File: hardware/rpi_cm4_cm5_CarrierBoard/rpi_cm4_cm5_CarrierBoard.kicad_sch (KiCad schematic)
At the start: 0 parts

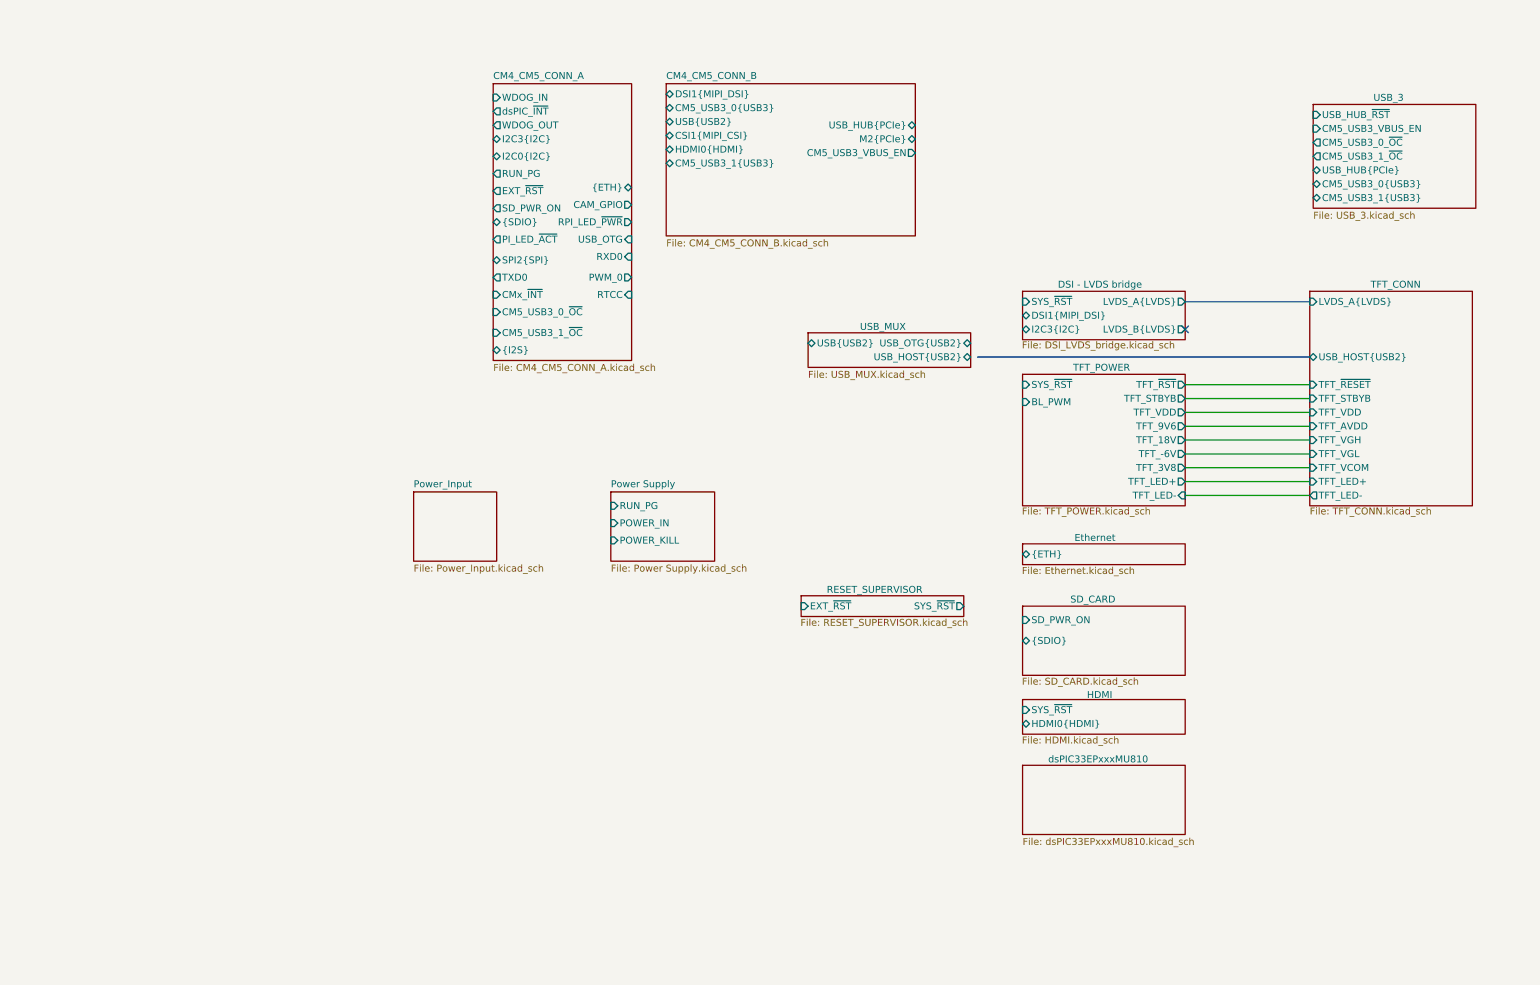
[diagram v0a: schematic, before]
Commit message: Add dsPIC sheet
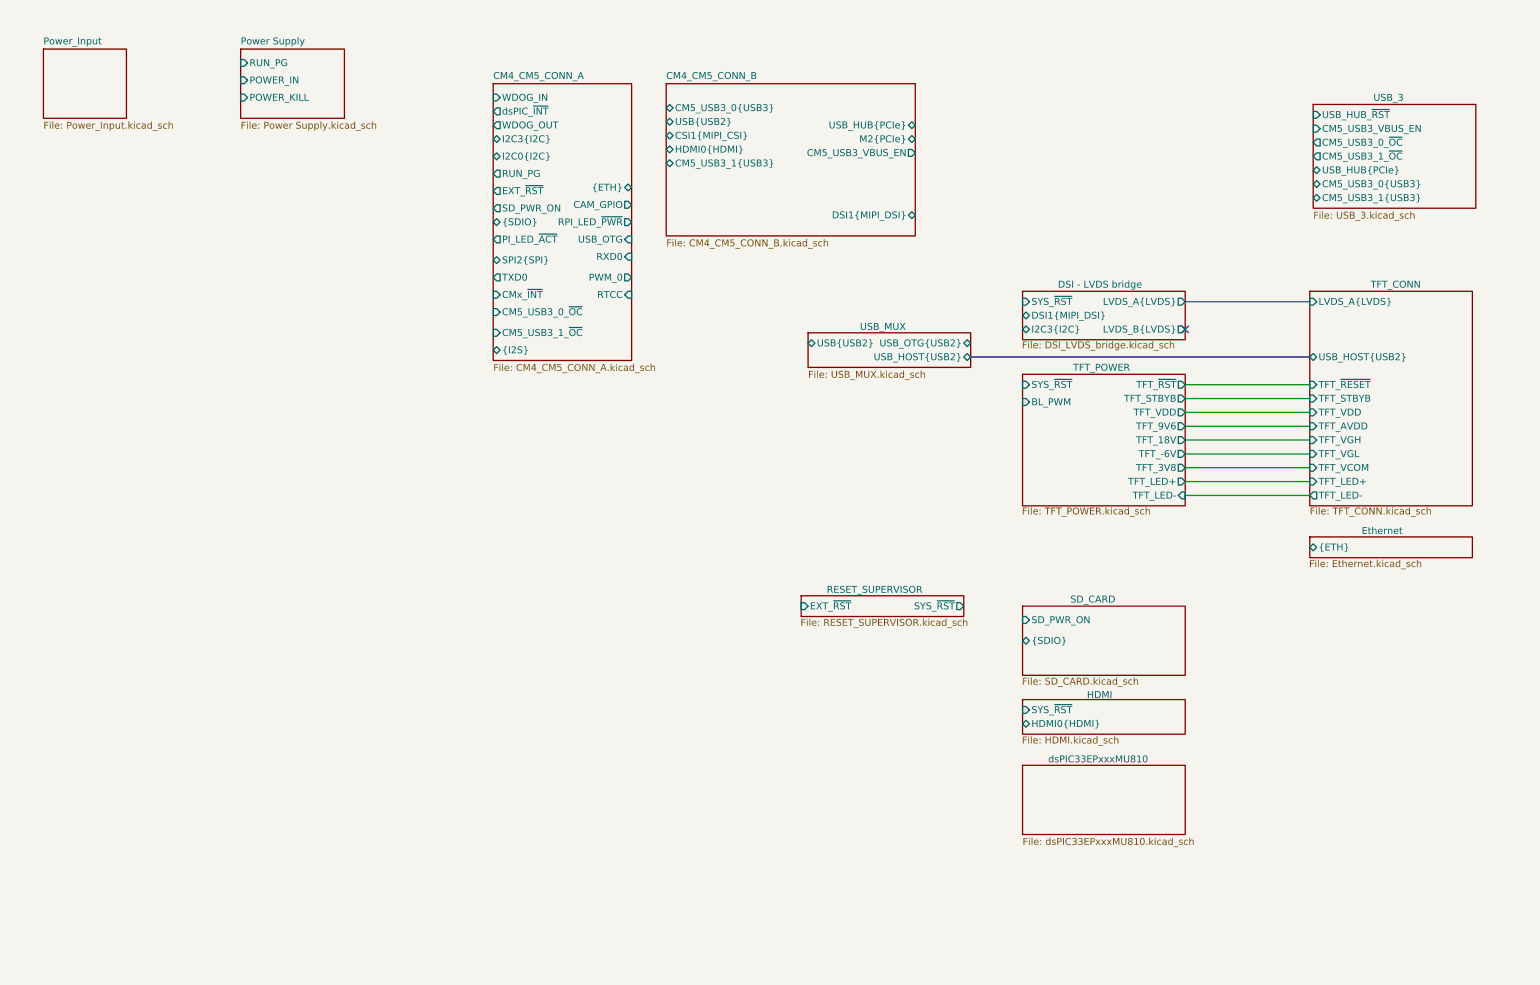
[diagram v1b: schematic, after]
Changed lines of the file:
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@@
-		)
-	)
-	(bus
-		(pts
-			(xy 190.5 75.565) (xy 251.46 75.565)
-		)
-		(stroke
-			(width 0)
-			(type default)
 		)
 	)
@@
 		(pts
 			(xy 228.6 100.965) (xy 251.46 100.965)
+		)
+		(stroke
+			(width 0)
+			(type default)
+		)
+	)
+	(bus
+		(pts
+			(xy 189.23 75.565) (xy 251.46 75.565)
 		)
 		(stroke
@@
 		)
 		(pin "DSI1{MIPI_DSI}" bidirectional
-			(at 133.35 27.305 180)
-			(effects
-				(font
-					(size 1.27 1.27)
-				)
-				(justify left)
+			(at 179.07 49.53 0)
+			(effects
+				(font
+					(size 1.27 1.27)
+				)
+				(justify right)
 			)
 		)
@@
 	)
 	(sheet
-		(at 86.995 100.33)
+		(at 19.05 19.05)
 		(size 15.24 12.7)
 		(exclude_from_sim no)
@@
 		)
 		(property "Sheetname" "Power_Input"
-			(at 86.995 99.6184 0)
+			(at 19.05 18.3384 0)
 			(effects
 				(font
@@
 		)
 		(property "Sheetfile" "Power_Input.kicad_sch"
-			(at 86.995 113.6146 0)
+			(at 19.05 32.3346 0)
 			(effects
 				(font
@@
 	)
 	(sheet
-		(at 198.755 109.855)
+		(at 251.46 108.585)
 		(size 29.845 3.81)
 		(exclude_from_sim no)
@@
 		)
 		(property "Sheetname" "Ethernet"
-			(at 208.28 109.474 0)
+			(at 260.985 108.204 0)
 			(effects
 				(font
@@
 		)
 		(property "Sheetfile" "Ethernet.kicad_sch"
-			(at 198.628 114.046 0)
+			(at 251.333 112.776 0)
 			(effects
 				(font
@@
 		)
 		(pin "{ETH}" bidirectional
-			(at 198.755 111.76 180)
+			(at 251.46 110.49 180)
 			(effects
 				(font
@@
 	)
 	(sheet
-		(at 123.19 100.33)
+		(at 55.245 19.05)
 		(size 19.05 12.7)
 		(exclude_from_sim no)
@@
 		)
 		(property "Sheetname" "Power Supply"
-			(at 123.19 99.6184 0)
+			(at 55.245 18.3384 0)
 			(effects
 				(font
@@
 		)
 		(property "Sheetfile" "Power Supply.kicad_sch"
-			(at 123.19 113.6146 0)
+			(at 55.245 32.3346 0)
 			(effects
 				(font
@@
 		)
 		(pin "RUN_PG" input
-			(at 123.19 102.87 180)
+			(at 55.245 21.59 180)
 			(effects
 				(font
@@
 		)
 		(pin "POWER_KILL" input
-			(at 123.19 109.22 180)
+			(at 55.245 27.94 180)
 			(effects
 				(font
@@
 		)
 		(pin "POWER_IN" input
-			(at 123.19 106.045 180)
-			(effects
-				(font
+			(at 55.245 24.765 180)
+			(effects
+				(font

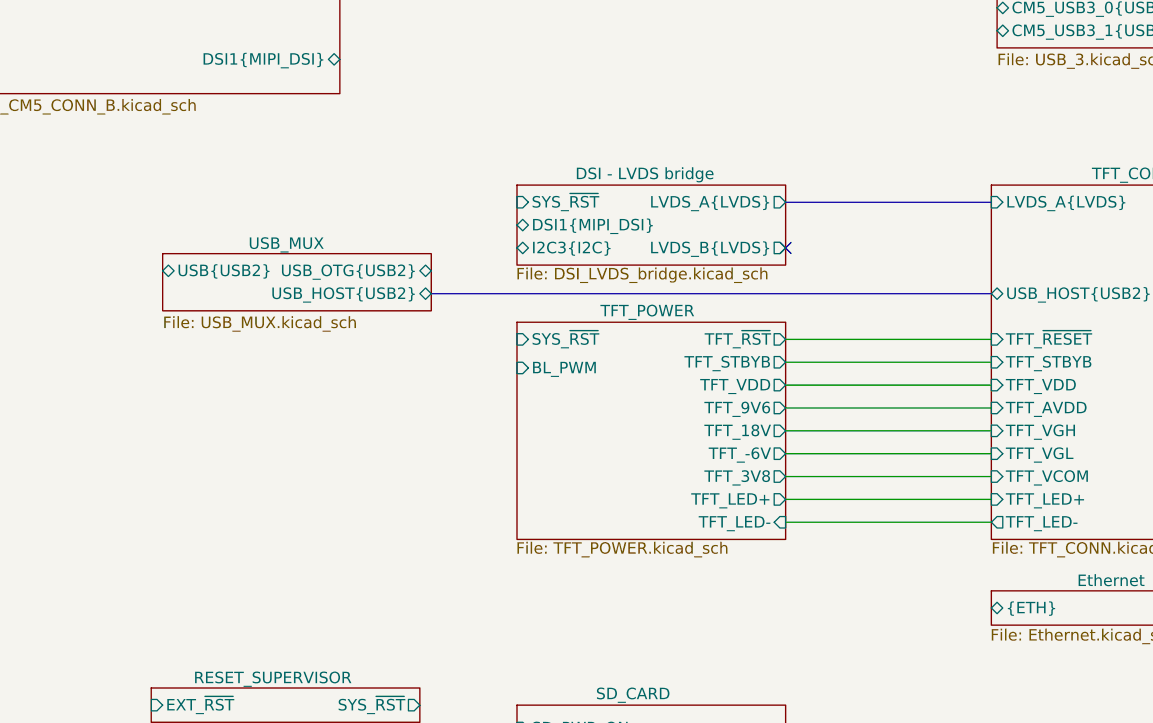
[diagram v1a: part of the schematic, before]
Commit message: Add power-up and power kill sequences Modify schematics to add net classes for DiffPairs
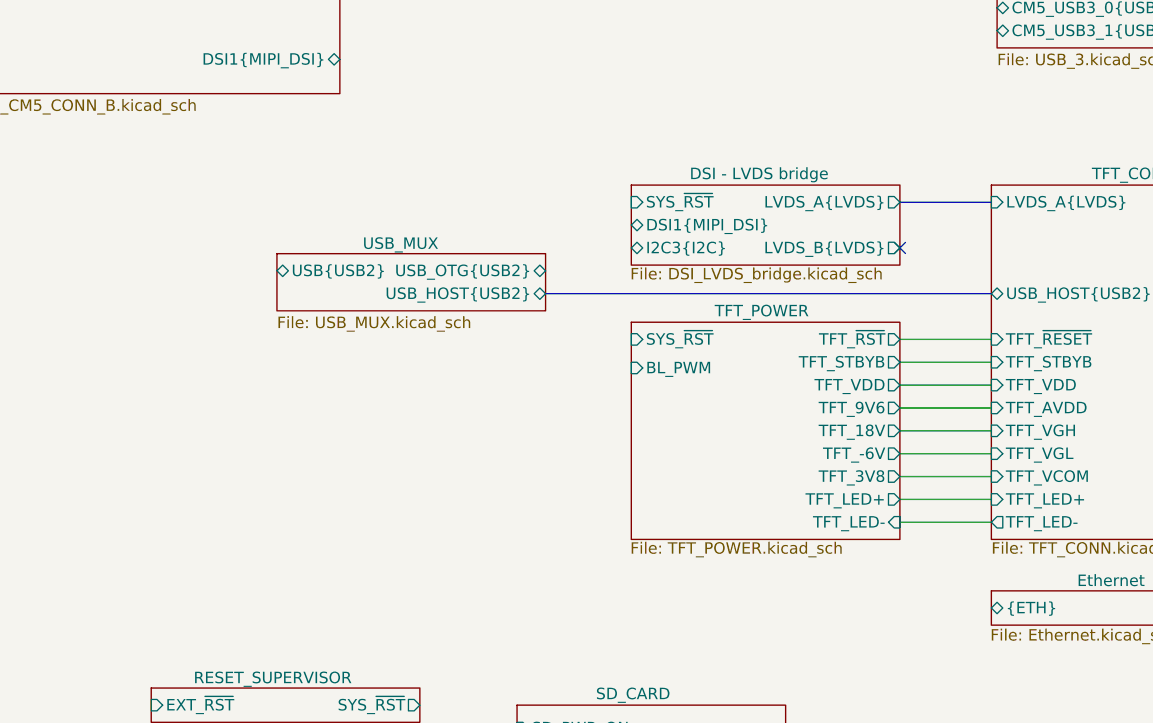
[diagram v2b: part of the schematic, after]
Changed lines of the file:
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@@
 	)
 	(no_connect
-		(at 228.6 70.485)
-	)
-	(wire
-		(pts
-			(xy 228.6 83.185) (xy 251.46 83.185)
-		)
-		(stroke
-			(width 0)
-			(type default)
-		)
-	)
-	(wire
-		(pts
-			(xy 228.6 90.805) (xy 251.46 90.805)
-		)
-		(stroke
-			(width 0)
-			(type default)
-		)
-	)
-	(wire
-		(pts
-			(xy 228.6 88.265) (xy 251.46 88.265)
+		(at 241.3 70.485)
+	)
+	(wire
+		(pts
+			(xy 241.3 83.185) (xy 251.46 83.185)
+		)
+		(stroke
+			(width 0)
+			(type default)
+		)
+	)
+	(wire
+		(pts
+			(xy 241.3 90.805) (xy 251.46 90.805)
+		)
+		(stroke
+			(width 0)
+			(type default)
+		)
+	)
+	(wire
+		(pts
+			(xy 241.3 88.265) (xy 251.46 88.265)
 		)
 		(stroke
@@
 	(bus
 		(pts
-			(xy 228.6 65.405) (xy 251.46 65.405)
-		)
-		(stroke
-			(width 0)
-			(type default)
-		)
-	)
-	(wire
-		(pts
-			(xy 228.6 100.965) (xy 251.46 100.965)
+			(xy 241.3 65.405) (xy 251.46 65.405)
+		)
+		(stroke
+			(width 0)
+			(type default)
+		)
+	)
+	(wire
+		(pts
+			(xy 241.3 100.965) (xy 251.46 100.965)
 		)
 		(stroke
@@
 	(bus
 		(pts
-			(xy 189.23 75.565) (xy 251.46 75.565)
-		)
-		(stroke
-			(width 0)
-			(type default)
-		)
-	)
-	(wire
-		(pts
-			(xy 228.6 98.425) (xy 251.46 98.425)
-		)
-		(stroke
-			(width 0)
-			(type default)
-		)
-	)
-	(wire
-		(pts
-			(xy 228.6 93.345) (xy 251.46 93.345)
-		)
-		(stroke
-			(width 0)
-			(type default)
-		)
-	)
-	(wire
-		(pts
-			(xy 228.6 80.645) (xy 251.46 80.645)
-		)
-		(stroke
-			(width 0)
-			(type default)
-		)
-	)
-	(wire
-		(pts
-			(xy 228.6 95.885) (xy 251.46 95.885)
-		)
-		(stroke
-			(width 0)
-			(type default)
-		)
-	)
-	(wire
-		(pts
-			(xy 228.6 85.725) (xy 251.46 85.725)
+			(xy 201.93 75.565) (xy 251.46 75.565)
+		)
+		(stroke
+			(width 0)
+			(type default)
+		)
+	)
+	(wire
+		(pts
+			(xy 241.3 98.425) (xy 251.46 98.425)
+		)
+		(stroke
+			(width 0)
+			(type default)
+		)
+	)
+	(wire
+		(pts
+			(xy 241.3 93.345) (xy 251.46 93.345)
+		)
+		(stroke
+			(width 0)
+			(type default)
+		)
+	)
+	(wire
+		(pts
+			(xy 241.3 80.645) (xy 251.46 80.645)
+		)
+		(stroke
+			(width 0)
+			(type default)
+		)
+	)
+	(wire
+		(pts
+			(xy 241.3 95.885) (xy 251.46 95.885)
+		)
+		(stroke
+			(width 0)
+			(type default)
+		)
+	)
+	(wire
+		(pts
+			(xy 241.3 85.725) (xy 251.46 85.725)
 		)
 		(stroke
@@
 	)
 	(sheet
-		(at 198.755 78.74)
+		(at 211.455 78.74)
 		(size 29.845 24.13)
 		(exclude_from_sim no)
@@
 		)
 		(property "Sheetname" "TFT_POWER"
-			(at 208.026 78.232 0)
+			(at 220.726 78.232 0)
 			(effects
 				(font
@@
 		)
 		(property "Sheetfile" "TFT_POWER.kicad_sch"
-			(at 198.628 103.124 0)
+			(at 211.328 103.124 0)
 			(effects
 				(font
@@
 		)
 		(pin "BL_PWM" input
-			(at 198.755 83.82 180)
+			(at 211.455 83.82 180)
 			(effects
 				(font
@@
 		)
 		(pin "TFT_3V8" output
-			(at 228.6 95.885 0)
+			(at 241.3 95.885 0)
 			(effects
 				(font
@@
 		)
 		(pin "TFT_LED-" input
-			(at 228.6 100.965 0)
+			(at 241.3 100.965 0)
 			(effects
 				(font
@@
 		)
 		(pin "TFT_LED+" output
-			(at 228.6 98.425 0)
+			(at 241.3 98.425 0)
 			(effects
 				(font
@@
 		)
 		(pin "TFT_~{RST}" output
-			(at 228.6 80.645 0)
+			(at 241.3 80.645 0)
 			(effects
 				(font
@@
 		)
 		(pin "TFT_9V6" output
-			(at 228.6 88.265 0)
+			(at 241.3 88.265 0)
 			(effects
 				(font
@@
 		)
 		(pin "TFT_STBYB" output
-			(at 228.6 83.185 0)
+			(at 241.3 83.185 0)
 			(effects
 				(font
@@
 		)
 		(pin "SYS_~{RST}" input
-			(at 198.755 80.645 180)
+			(at 211.455 80.645 180)
 			(effects
 				(font
@@
 		)
 		(pin "TFT_-6V" output
-			(at 228.6 93.345 0)
+			(at 241.3 93.345 0)
 			(effects
 				(font
@@
 		)
 		(pin "TFT_18V" output
-			(at 228.6 90.805 0)
+			(at 241.3 90.805 0)
 			(effects
 				(font
@@
 		)
 		(pin "TFT_VDD" output
-			(at 228.6 85.725 0)
+			(at 241.3 85.725 0)
 			(effects
 				(font
@@
 	)
 	(sheet
-		(at 159.385 71.12)
+		(at 172.085 71.12)
 		(size 29.845 6.35)
 		(exclude_from_sim no)
@@
 		)
 		(property "Sheetname" "USB_MUX"
-			(at 168.91 70.739 0)
+			(at 181.61 70.739 0)
 			(effects
 				(font
@@
 		)
 		(property "Sheetfile" "USB_MUX.kicad_sch"
-			(at 159.385 78.0546 0)
+			(at 172.085 78.0546 0)
 			(effects
 				(font
@@
 		)
 		(pin "USB{USB2}" bidirectional
-			(at 159.385 73.025 180)
+			(at 172.085 73.025 180)
 			(effects
 				(font
@@
 		)
 		(pin "USB_OTG{USB2}" bidirectional
-			(at 189.23 73.025 0)
+			(at 201.93 73.025 0)
 			(effects
 				(font
@@
 		)
 		(pin "USB_HOST{USB2}" bidirectional
-			(at 189.23 75.565 0)
+			(at 201.93 75.565 0)
 			(effects
 				(font
@@
 	)
 	(sheet
-		(at 198.755 63.5)
+		(at 211.455 63.5)
 		(size 29.845 8.89)
 		(exclude_from_sim no)
@@
 		)
 		(property "Sheetname" "DSI - LVDS bridge"
-			(at 205.232 62.992 0)
+			(at 217.932 62.992 0)
 			(effects
 				(font
@@
 		)
 		(property "Sheetfile" "DSI_LVDS_bridge.kicad_sch"
-			(at 198.628 72.644 0)
+			(at 211.328 72.644 0)
 			(effects
 				(font
@@
 		)
 		(pin "SYS_~{RST}" input
-			(at 198.755 65.405 180)
+			(at 211.455 65.405 180)
 			(effects
 				(font
@@
 		)
 		(pin "DSI1{MIPI_DSI}" bidirectional
-			(at 198.755 67.945 180)
+			(at 211.455 67.945 180)
 			(effects
 				(font
@@
 		)
 		(pin "I2C3{I2C}" bidirectional
-			(at 198.755 70.485 180)
+			(at 211.455 70.485 180)
 			(effects
 				(font
@@
 		)
 		(pin "LVDS_A{LVDS}" output
-			(at 228.6 65.405 0)
+			(at 241.3 65.405 0)
 			(effects
 				(font
@@
 		)
 		(pin "LVDS_B{LVDS}" output
-			(at 228.6 70.485 0)
-			(effects
-				(font
+			(at 241.3 70.485 0)
+			(effects
+				(font
